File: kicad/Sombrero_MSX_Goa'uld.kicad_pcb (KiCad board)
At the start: 2 copper layers, 53.3 x 81.3 mm, 16 parts, among them J1 Z80CPU, U1 74AHCT373, U2 74AHCT373, U3 SN74LVC245AN, U4 SN74LVC245AN, U5 SN74LVC245AN, U6 Tang_Nano_20k

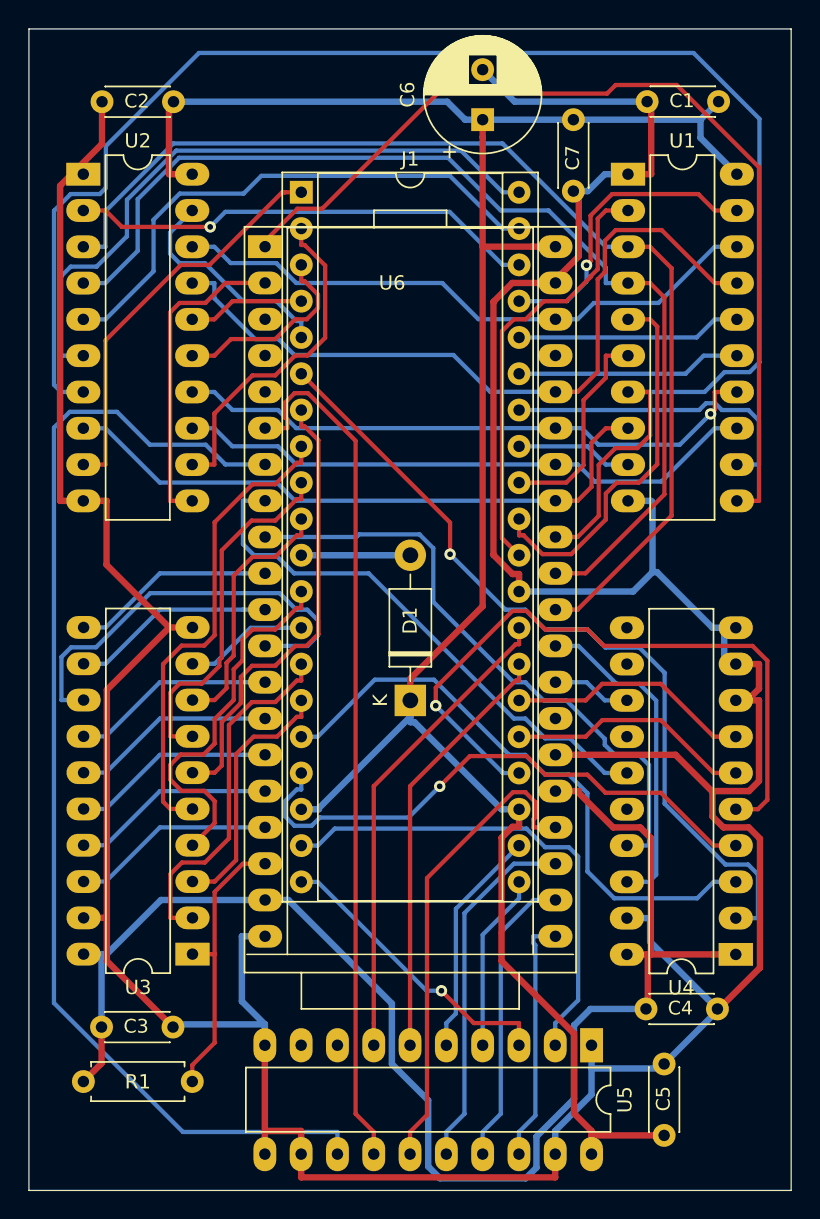
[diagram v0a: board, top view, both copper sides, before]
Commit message: Removed NMI, BUSRQ pins to avoid overheating of U4 due to voltage >> 5V Fixed name 74HCT373
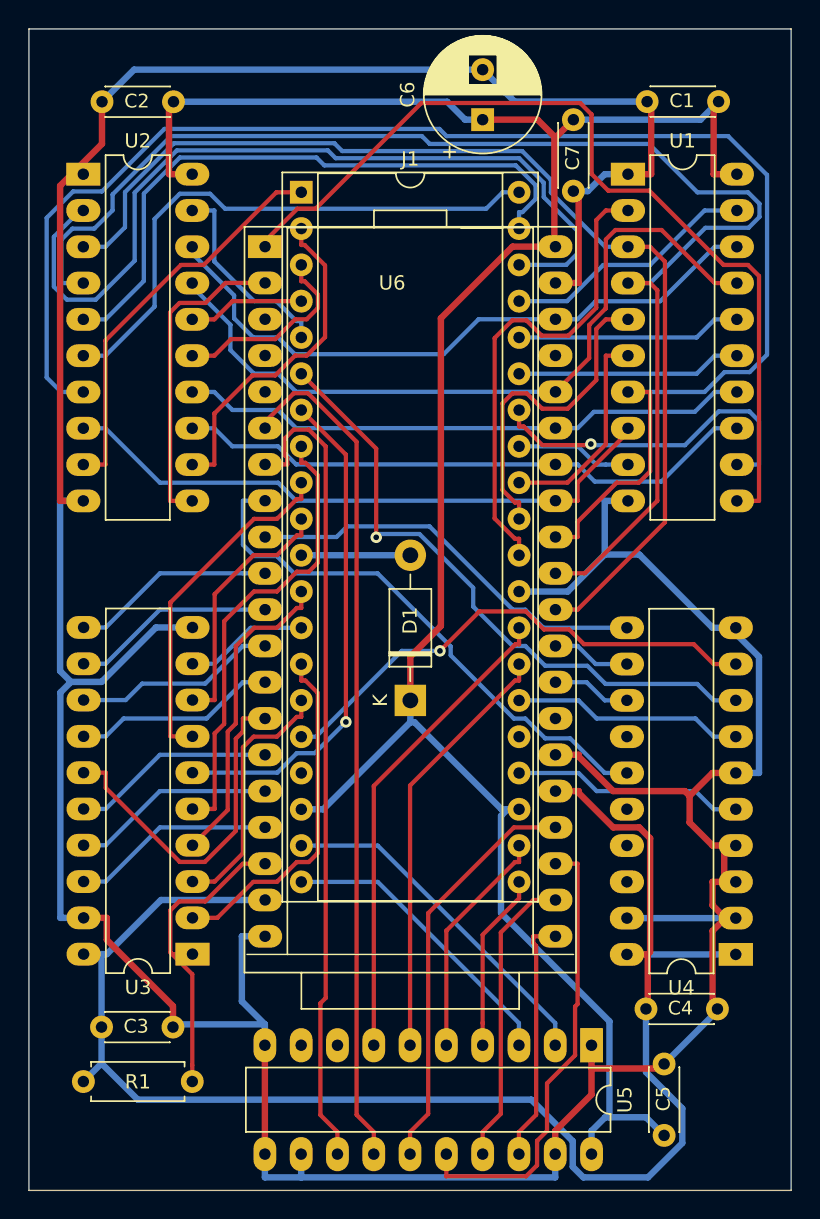
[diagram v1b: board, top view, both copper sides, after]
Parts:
- U1, U2: value 74AHCT373 -> 74HCT373
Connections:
- U4 pad 11: unconnected-(U4-Pad11) -> INT_33
- U4 pad 12: unconnected-(U4-Pad12) -> CLOCK_33
- U4 pad 17: INT_33 -> unconnected-(U4-Pad17)
- U4 pad 18: CLOCK_33 -> unconnected-(U4-Pad18)
- U4 pad 2: CLOCK -> GND
- U4 pad 3: INT -> GND
- U4 pad 4: NMI -> GND
- U4 pad 6: BUSRQ -> GND
- U4 pad 8: GND -> CLOCK
- U4 pad 9: GND -> INT
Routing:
- net NMI: track 40.1 -> 0.00 mm, vias 1 -> 0
- net WAIT: track 48.2 -> 16.2 mm, vias 1 -> 0
- net A8: track 32.9 -> 59.4 mm, vias 1 -> 0
- net RFSH_33: track 82.1 -> 57.2 mm
- net MP1_33: track 74.8 -> 97.3 mm
- net CLOCK_33: track 23.1 -> 5.53 mm
- net BUSRQ: track 17.2 -> 0.00 mm
- net D5_33: track 30.2 -> 14.3 mm
- net INT_33: track 43.3 -> 28.6 mm
- net CLOCK: track 57.7 -> 44.5 mm
- net D3_33: track 14.3 -> 24.4 mm
- net MERQ: track 34.5 -> 24.5 mm
- net VCC_3V3: track 100.6 -> 109.4 mm
- net MP2_33: track 115.4 -> 108.1 mm
- net RD_33: track 25.2 -> 32.0 mm
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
